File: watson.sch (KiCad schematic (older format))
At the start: 44 parts, among them P1 CONN_1, P2 CONN_1, P3 CONN_1, P4 CONN_1, P5 BNC, P6 CONN_1, U1 78L05, U2 79L05, U3 AD603, U4 BPF, U5 AD8307

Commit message: Renumbered components in schematic and added capacitors to module file.
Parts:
- renumbered C14 to C10, C3 to C11, C11 to C12, C4 to C13, C12 to C14, C16 to C15, C19 to C16, C5 to C18, C13 to C19, C6 to C2, C8 to C3, C2 to C4, C7 to C5, C9 to C6, C10 to C7, C15 to C8, C18 to C9, L5 to L1, L1 to L5, R2 to R1, R3 to R2, R5 to R3, R6 to R4, R4 to R5, R7 to R6, R8 to R7, R1 to R8, U4 to U3, U3 to U4
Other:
- note added: "50Ω input\n-105 dBm to +15 dBm"
- moved on the sheet: C18
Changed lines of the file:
@@
-EESchema Schematic File Version 2  date Friday, September 20, 2013 10:10:59 PM
+EESchema Schematic File Version 2  date Saturday, September 21, 2013 03:33:47 PM
 LIBS:watson
-LIBS:watson-cache
 EELAYER 27 0
 EELAYER END
@@
 encoding utf-8
 Sheet 1 1
-Title "Kicad Test Page"
-Date "19 sep 2013"
+Title "Watson - A 10.7 MHz Power Meter"
+Date "21 sep 2013"
 Rev "A"
-Comp "Pare Technologies"
+Comp "Copyright 2013 - Pare Technologies"
 Comment1 ""
 Comment2 ""
@@
 $EndDescr
 $Comp
-L INDUCTOR L5
+L INDUCTOR L1
 U 1 1 5212B401
 P 4140 3870
-F 0 "L5" V 4090 3870 40  0000 C CNN
+F 0 "L1" V 4090 3870 40  0000 C CNN
 F 1 "750nH" V 4240 3870 40  0000 C CNN
 F 2 "~" H 4140 3870 60  0000 C CNN
@@
 $EndComp
 $Comp
-L C C14
+L C C10
 U 1 1 5212DB59
 P 4140 4370
-F 0 "C14" H 4140 4470 40  0000 L CNN
+F 0 "C10" H 4140 4470 40  0000 L CNN
 F 1 "150p" H 4146 4285 40  0000 L CNN
 F 2 "~" H 4178 4220 30  0000 C CNN
@@
 $EndComp
 $Comp
-L R R3
+L R R2
 U 1 1 521421EA
 P 1910 4330
-F 0 "R3" V 1990 4330 40  0000 C CNN
+F 0 "R2" V 1990 4330 40  0000 C CNN
 F 1 "28k" V 1917 4331 40  0000 C CNN
 F 2 "~" V 1840 4330 30  0000 C CNN
@@
 $EndComp
 $Comp
-L R R2
+L R R1
 U 1 1 521421F7
 P 1600 4030
-F 0 "R2" V 1680 4030 40  0000 C CNN
+F 0 "R1" V 1680 4030 40  0000 C CNN
 F 1 "187k" V 1607 4031 40  0000 C CNN
 F 2 "~" V 1530 4030 30  0000 C CNN
@@
 $EndComp
 $Comp
-L R R5
+L R R3
 U 1 1 521421FD
 P 6300 3720
-F 0 "R5" V 6380 3720 40  0000 C CNN
+F 0 "R3" V 6380 3720 40  0000 C CNN
 F 1 "330" V 6307 3721 40  0000 C CNN
 F 2 "~" V 6230 3720 30  0000 C CNN
@@
 $EndComp
 $Comp
-L R R6
+L R R4
 U 1 1 52142203
 P 7440 4320
-F 0 "R6" V 7520 4320 40  0000 C CNN
+F 0 "R4" V 7520 4320 40  0000 C CNN
 F 1 "464" V 7447 4321 40  0000 C CNN
 F 2 "~" V 7370 4320 30  0000 C CNN
@@
 $EndComp
 $Comp
-L R R1
+L R R8
 U 1 1 52142209
 P 1560 6670
-F 0 "R1" V 1640 6670 40  0000 C CNN
+F 0 "R8" V 1640 6670 40  0000 C CNN
 F 1 "4.7" V 1567 6671 40  0000 C CNN
 F 2 "~" V 1490 6670 30  0000 C CNN
@@
 $EndComp
 $Comp
-L C C5
+L C C18
 U 1 1 52142277
-P 1900 6870
-F 0 "C5" H 1900 6970 40  0000 L CNN
-F 1 "0.1u" H 1906 6785 40  0000 L CNN
-F 2 "~" H 1938 6720 30  0000 C CNN
-F 3 "~" H 1900 6870 60  0000 C CNN
-	1    1900 6870
+P 1850 6870
+F 0 "C18" H 1850 6970 40  0000 L CNN
+F 1 "0.1u" H 1856 6785 40  0000 L CNN
+F 2 "~" H 1888 6720 30  0000 C CNN
+F 3 "~" H 1850 6870 60  0000 C CNN
+	1    1850 6870
 	-1   0    0    1
 $EndComp
@@
 L GND #PWR01
 U 1 1 5214229C
-P 1900 7130
-F 0 "#PWR01" H 1900 7130 30  0001 C CNN
-F 1 "GND" H 1900 7060 30  0001 C CNN
-F 2 "" H 1900 7130 60  0000 C CNN
-F 3 "" H 1900 7130 60  0000 C CNN
-	1    1900 7130
+P 1850 7130
+F 0 "#PWR01" H 1850 7130 30  0001 C CNN
+F 1 "GND" H 1850 7060 30  0001 C CNN
+F 2 "" H 1850 7130 60  0000 C CNN
+F 3 "" H 1850 7130 60  0000 C CNN
+	1    1850 7130
 	1    0    0    -1
 $EndComp
@@
 $EndComp
 $Comp
-L R R8
+L R R7
 U 1 1 5214240B
 P 8290 5220
-F 0 "R8" V 8370 5220 40  0000 C CNN
+F 0 "R7" V 8370 5220 40  0000 C CNN
 F 1 "80.6k" V 8297 5221 40  0000 C CNN
 F 2 "~" V 8220 5220 30  0000 C CNN
@@
 $EndComp
 $Comp
-L R R7
+L R R6
 U 1 1 5214241D
 P 7790 5470
-F 0 "R7" V 7870 5470 40  0000 C CNN
+F 0 "R6" V 7870 5470 40  0000 C CNN
 F 1 "20k" V 7797 5471 40  0000 C CNN
 F 2 "~" V 7720 5470 30  0000 C CNN
@@
 $EndComp
 $Comp
-L R R4
+L R R5
 U 1 1 5214271F
 P 4540 5820
-F 0 "R4" V 4620 5820 40  0000 C CNN
+F 0 "R5" V 4620 5820 40  0000 C CNN
 F 1 "100k" V 4547 5821 40  0000 C CNN
 F 2 "~" V 4470 5820 30  0000 C CNN
@@
 $EndComp
 $Comp
-L C C6
+L C C2
 U 1 1 5224CC42
 P 1960 2330
-F 0 "C6" H 1960 2430 40  0000 L CNN
+F 0 "C2" H 1960 2430 40  0000 L CNN
 F 1 ".1u" H 1966 2245 40  0000 L CNN
 F 2 "~" H 1998 2180 30  0000 C CNN
@@
 $EndComp
 $Comp
-L C C3
+L C C11
 U 1 1 5224CF97
 P 1820 5020
-F 0 "C3" H 1820 5120 40  0000 L CNN
+F 0 "C11" H 1820 5120 40  0000 L CNN
 F 1 "0.1u" H 1826 4935 40  0000 L CNN
 F 2 "~" H 1858 4870 30  0000 C CNN
@@
 $EndComp
 $Comp
-L C C15
+L C C8
 U 1 1 5224D0D5
 P 4840 4970
-F 0 "C15" H 4840 5070 40  0000 L CNN
+F 0 "C8" H 4840 5070 40  0000 L CNN
 F 1 "C" H 4846 4885 40  0000 L CNN
 F 2 "~" H 4878 4820 30  0000 C CNN
@@
 $EndComp
 $Comp
-L C C12
+L C C14
 U 1 1 5224D219
 P 2260 5880
-F 0 "C12" H 2260 5980 40  0000 L CNN
+F 0 "C14" H 2260 5980 40  0000 L CNN
 F 1 "C" H 2266 5795 40  0000 L CNN
 F 2 "~" H 2298 5730 30  0000 C CNN
@@
 $EndComp
 $Comp
-L C C16
+L C C15
 U 1 1 5224D363
 P 6300 4910
-F 0 "C16" H 6300 5010 40  0000 L CNN
+F 0 "C15" H 6300 5010 40  0000 L CNN
 F 1 "C" H 6306 4825 40  0000 L CNN
 F 2 "~" H 6338 4760 30  0000 C CNN
@@
 $EndComp
 $Comp
-L C C7
+L C C5
 U 1 1 522E6C59
 P 1960 3080
-F 0 "C7" H 1960 3180 40  0000 L CNN
+F 0 "C5" H 1960 3180 40  0000 L CNN
 F 1 "0.1u" H 1966 2995 40  0000 L CNN
 F 2 "~" H 1998 2930 30  0000 C CNN
@@
 $EndComp
 $Comp
-L CP1 C2
+L CP1 C4
 U 1 1 522FBB76
 P 1160 3080
-F 0 "C2" H 1210 3180 50  0000 L CNN
+F 0 "C4" H 1210 3180 50  0000 L CNN
 F 1 "33u" H 1210 2980 50  0000 L CNN
 F 2 "~" H 1160 3080 60  0000 C CNN
@@
 $EndComp
 $Comp
-L C C8
+L C C3
 U 1 1 52325A8C
 P 2160 2330
-F 0 "C8" H 2160 2430 40  0000 L CNN
+F 0 "C3" H 2160 2430 40  0000 L CNN
 F 1 "C" H 2166 2245 40  0000 L CNN
 F 2 "~" H 2198 2180 30  0000 C CNN
@@
 $EndComp
 $Comp
-L C C9
+L C C6
 U 1 1 52325AC8
 P 2160 3080
-F 0 "C9" H 2160 3180 40  0000 L CNN
+F 0 "C6" H 2160 3180 40  0000 L CNN
 F 1 "C" H 2166 2995 40  0000 L CNN
 F 2 "~" H 2198 2930 30  0000 C CNN
@@
 $EndComp
 $Comp
-L C C4
+L C C13
 U 1 1 52326254
 P 1840 5880
-F 0 "C4" H 1840 5980 40  0000 L CNN
+F 0 "C13" H 1840 5980 40  0000 L CNN
 F 1 "C" H 1846 5795 40  0000 L CNN
 F 2 "~" H 1878 5730 30  0000 C CNN
@@
 $EndComp
 $Comp
-L C C11
+L C C12
 U 1 1 523262F9
 P 2260 5020
-F 0 "C11" H 2260 5120 40  0000 L CNN
+F 0 "C12" H 2260 5120 40  0000 L CNN
 F 1 "C" H 2266 4935 40  0000 L CNN
 F 2 "~" H 2298 4870 30  0000 C CNN
@@
 $EndComp
 $Comp
-L C C13
+L C C19
 U 1 1 5232683C
 P 2340 6870
-F 0 "C13" H 2340 6970 40  0000 L CNN
+F 0 "C19" H 2340 6970 40  0000 L CNN
 F 1 "C" H 2346 6785 40  0000 L CNN
 F 2 "~" H 2378 6720 30  0000 C CNN
@@
 $EndComp
 $Comp
-L C C10
+L C C7
 U 1 1 5224CAFF
 P 2260 4310
-F 0 "C10" H 2260 4410 40  0000 L CNN
+F 0 "C7" H 2260 4410 40  0000 L CNN
 F 1 "C" H 2266 4225 40  0000 L CNN
 F 2 "~" H 2298 4160 30  0000 C CNN
@@
 VNEG
 $Comp
-L L L1
+L L L5
 U 1 1 523A56CE
 P 1040 6670
-F 0 "L1" V 1120 6670 40  0000 C CNN
+F 0 "L5" V 1120 6670 40  0000 C CNN
 F 1 "L" V 1040 6670 40  0000 C CNN
 F 2 "~" V 970 6670 30  0000 C CNN
@@
 VNEG
 $Comp
-L AD603 U3
+L AD603 U4
 U 1 1 5212DAF3
 P 5290 4070
-F 0 "U3" H 5040 3620 60  0000 C CNN
+F 0 "U4" H 5040 3620 60  0000 C CNN
 F 1 "AD603" H 5290 4070 60  0000 C CNN
 F 2 "" H 5290 4220 60  0000 C CNN
@@
 $EndComp
 $Comp
-L C C19
+L C C16
 U 1 1 523A5D90
 P 6560 4910
-F 0 "C19" H 6560 5010 40  0000 L CNN
+F 0 "C16" H 6560 5010 40  0000 L CNN
 F 1 "C" H 6566 4825 40  0000 L CNN
 F 2 "~" H 6598 4760 30  0000 C CNN
@@
 $EndComp
 $Comp
-L C C18
+L C C9
 U 1 1 523A5F48
 P 5130 4970
-F 0 "C18" H 5130 5070 40  0000 L CNN
+F 0 "C9" H 5130 5070 40  0000 L CNN
 F 1 "C" H 5136 4885 40  0000 L CNN
 F 2 "~" H 5168 4820 30  0000 C CNN
@@
 $EndComp
 $Comp
-L BPF U4
+L BPF U3
 U 1 1 523B8809
 P 6900 3370
-F 0 "U4" H 6850 3570 60  0000 C CNN
+F 0 "U3" H 6850 3570 60  0000 C CNN
 F 1 "BPF" H 6900 3170 60  0000 C CNN
 F 2 "~" H 6900 3420 60  0000 C CNN
@@
 Wire Wire Line
 	1810 6670 2740 6670
-Connection ~ 1900 6670
-Wire Wire Line
-	1900 7070 1900 7130
+Connection ~ 1850 6670
+Wire Wire Line
+	1850 7070 1850 7130
 Wire Wire Line
 	2340 7070 2340 7130
@@
 Wire Wire Line
 	6750 3470 6750 3630
+Text Notes 4400 3300 0    60   ~ 0
+50Ω input\n-105 dBm to +15 dBm
 $EndSCHEMATC

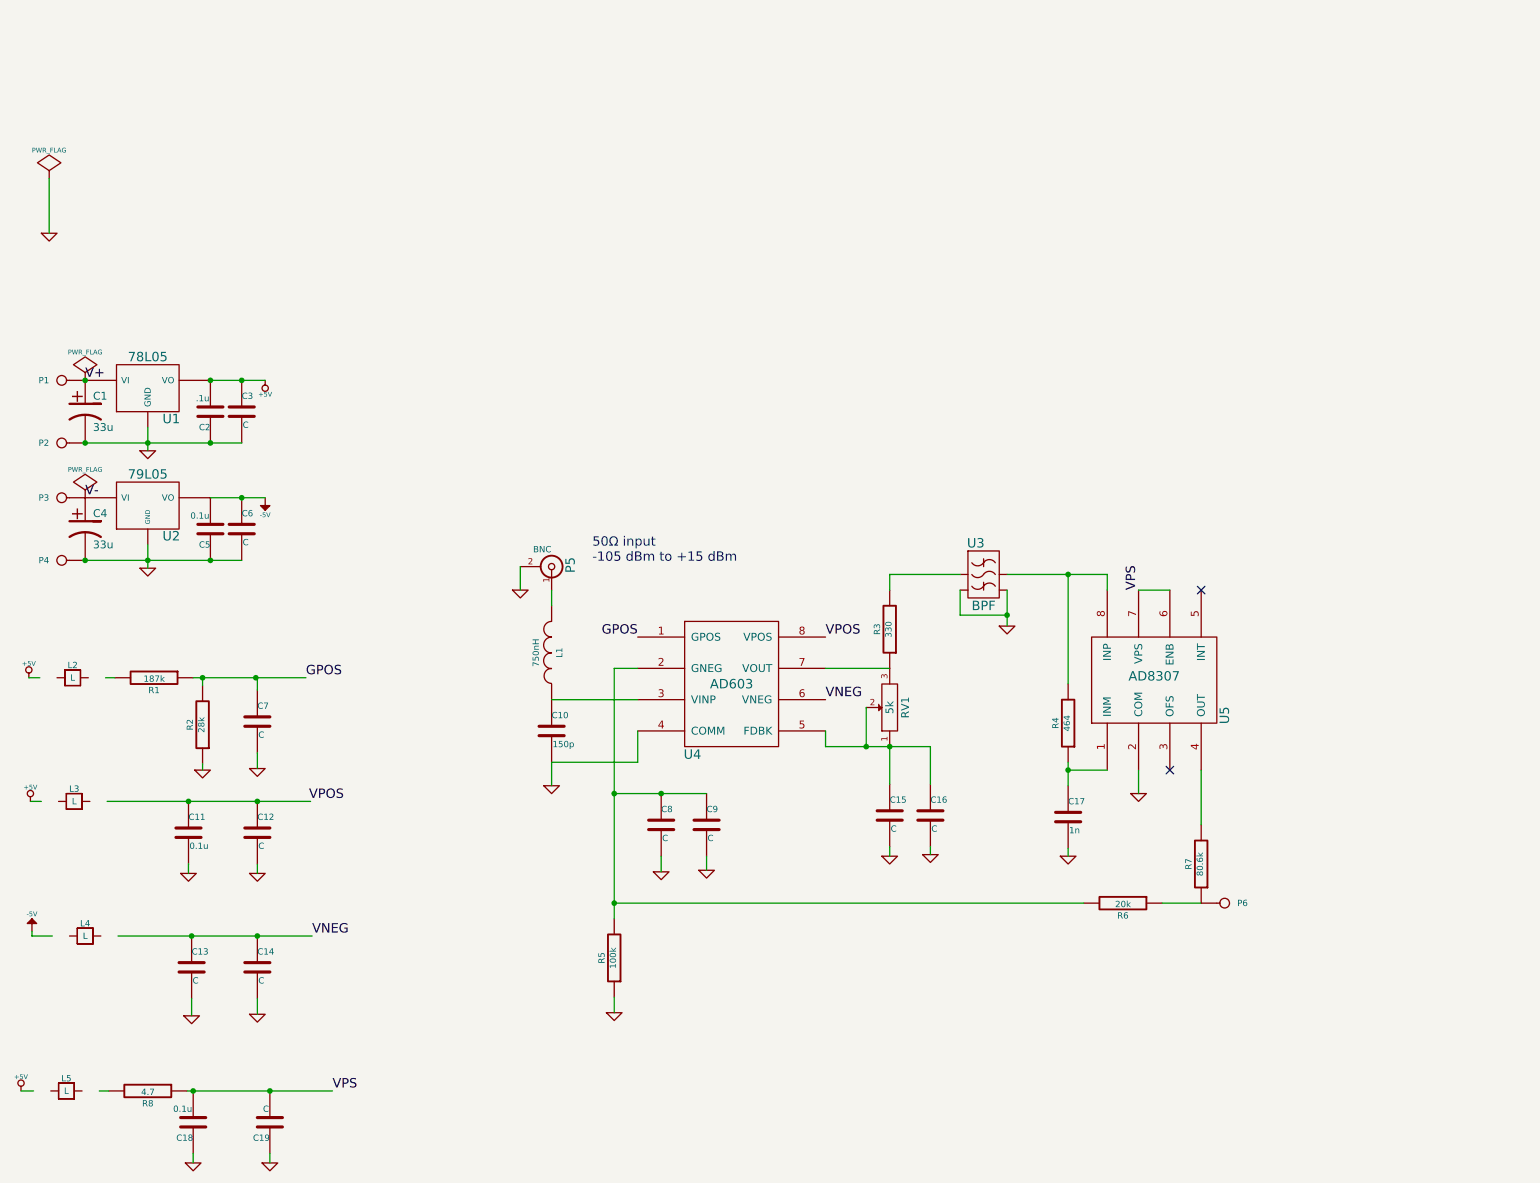
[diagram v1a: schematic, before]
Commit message: Schematic reworked.
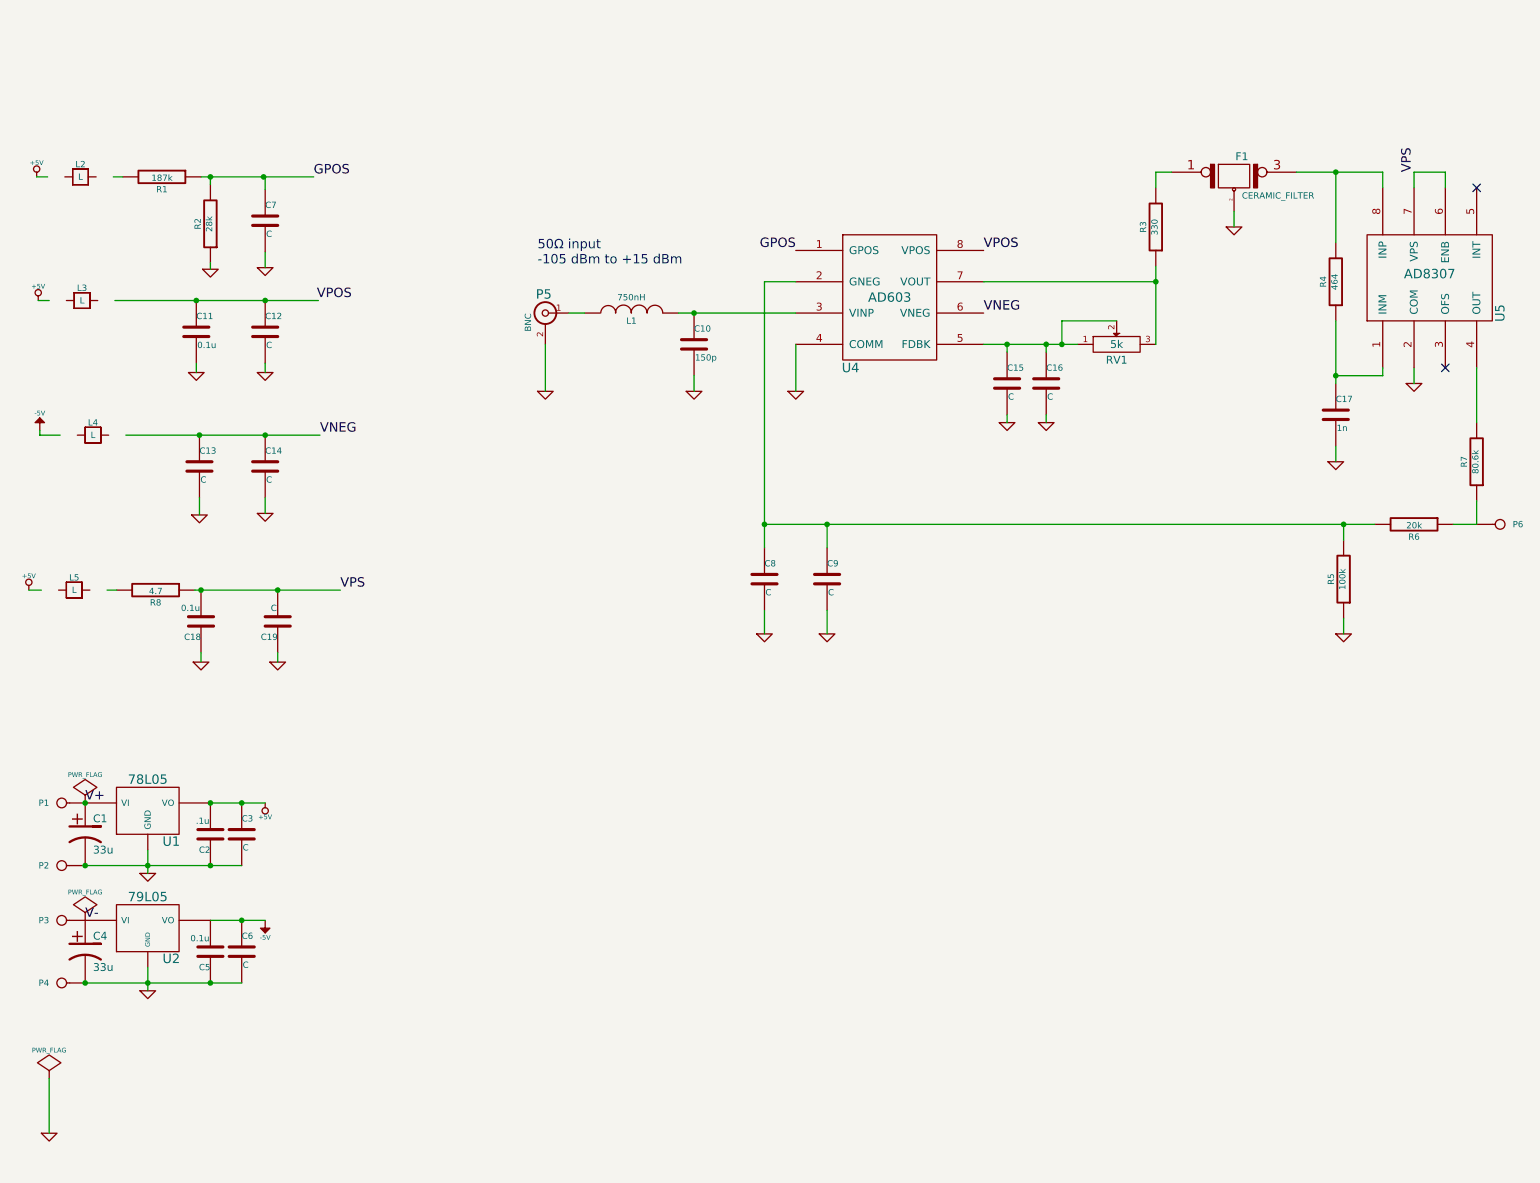
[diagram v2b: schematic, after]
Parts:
- removed U3: BPF, ~, symbol BPF
- added F1: CERAMIC_FILTER, ~, symbol CERAMIC_FILTER
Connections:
- wire segments 66 -> 69
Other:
- moved on the sheet: C1, C10, C11, C12, C13, C14, C15, C16, C17, C18, C19, C2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

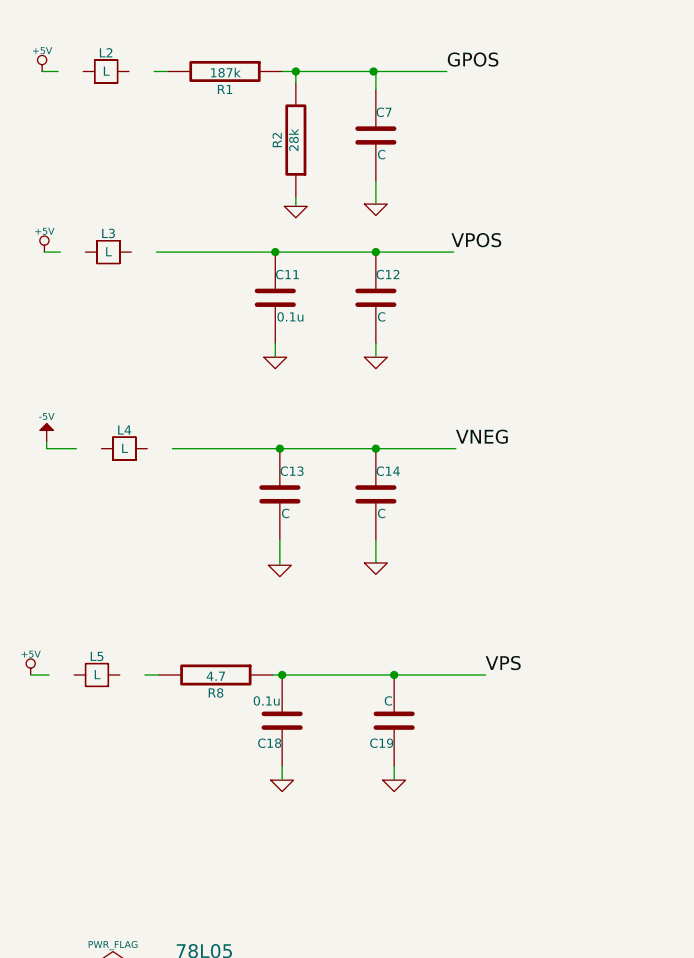
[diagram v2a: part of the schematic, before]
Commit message: Added ferrite bead module and created an autoplace PCB.
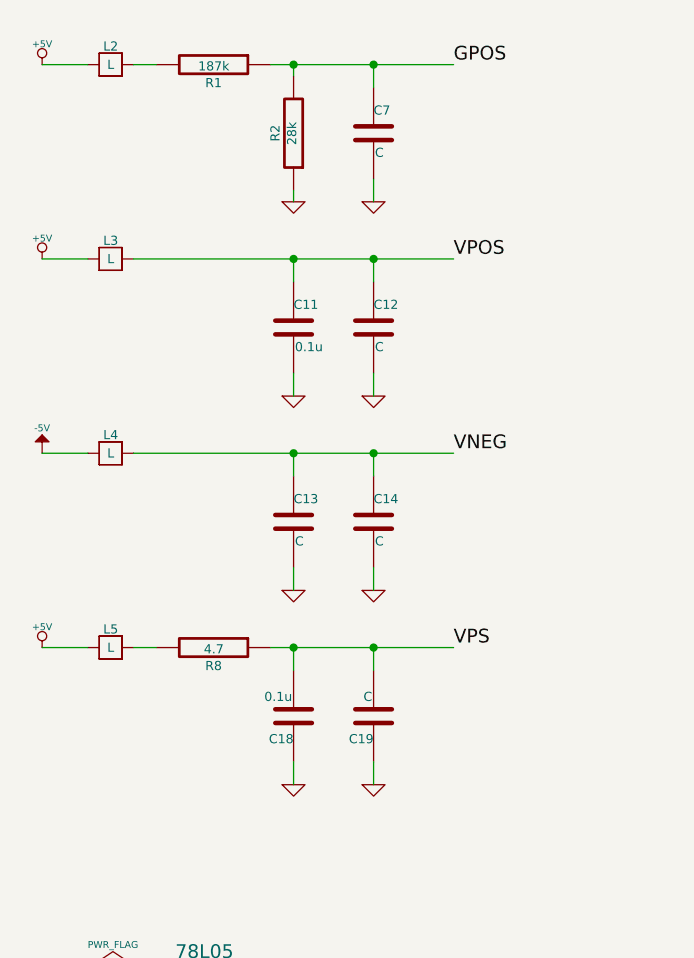
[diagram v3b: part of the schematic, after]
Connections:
- wire segments 69 -> 73
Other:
- moved on the sheet: C11, C12, C13, C14, C18, C19, L2, L3, L4, L5, R1, R2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
